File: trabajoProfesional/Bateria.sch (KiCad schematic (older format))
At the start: 28 parts, among them T1 MPMOS

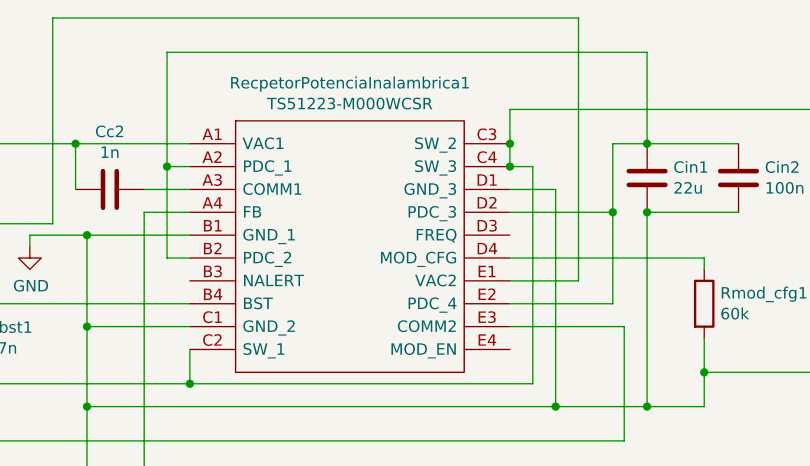
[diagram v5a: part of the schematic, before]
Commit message: achicamiento de placa a un cuarto del tamanio anterior
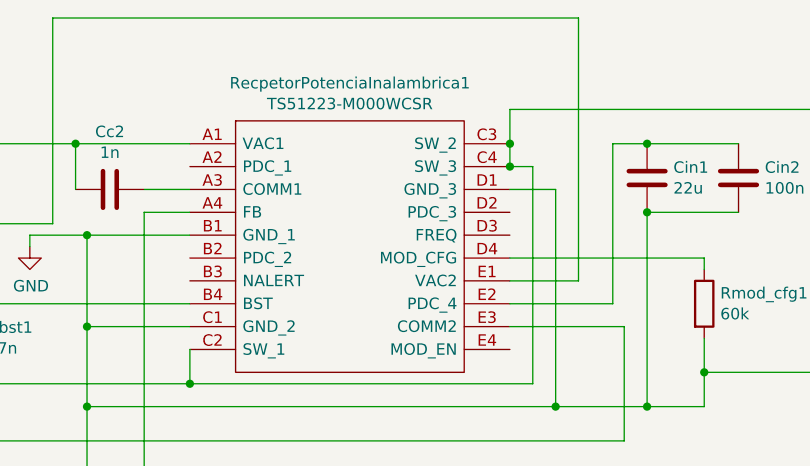
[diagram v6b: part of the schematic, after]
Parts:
- Cbat1, Cvin1: footprint Capacitor_SMD:C_Elec_3x5.4 -> Capacitor_SMD:C_0201_0603Metric
- Cc1, Cc2, Cin1, Cin2, Cout1, Cout2, Cout3, Cout4, Cs2: footprint Capacitor_SMD:CP_Elec_3x5.3 -> Capacitor_SMD:C_0201_0603Metric
- Lout1: footprint Inductor_SMD:L_7.3x7.3_H3.5 -> Inductor_SMD:L_0603_1608Metric_Pad1.05x0.95mm_HandSolder
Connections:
- net at Cin1.2, Cin2.2, RecpetorPotenciaInalambrica1.E2 (PDC_4): no longer RecpetorPotenciaInalambrica1.A2 (PDC_1), RecpetorPotenciaInalambrica1.B2 (PDC_2), RecpetorPotenciaInalambrica1.D2 (PDC_3)
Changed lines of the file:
@@
 F 0 "Cs2" V 1498 2200 50  0000 C CNN
 F 1 "10n" V 1589 2200 50  0000 C CNN
-F 2 "Capacitor_SMD:CP_Elec_3x5.3" H 1788 2050 50  0001 C CNN
+F 2 "Capacitor_SMD:C_0201_0603Metric" H 1788 2050 50  0001 C CNN
 F 3 "~" H 1750 2200 50  0001 C CNN
 	1    1750 2200
@@
 F 0 "Cc1" H 1435 3054 50  0000 R CNN
 F 1 "1n" H 1435 3145 50  0000 R CNN
-F 2 "Capacitor_SMD:CP_Elec_3x5.3" H 1588 2950 50  0001 C CNN
+F 2 "Capacitor_SMD:C_0201_0603Metric" H 1588 2950 50  0001 C CNN
 F 3 "~" H 1550 3100 50  0001 C CNN
 	1    1550 3100
@@
 F 0 "Cc2" V 3202 2400 50  0000 C CNN
 F 1 "1n" V 3111 2400 50  0000 C CNN
-F 2 "Capacitor_SMD:CP_Elec_3x5.3" H 2988 2250 50  0001 C CNN
+F 2 "Capacitor_SMD:C_0201_0603Metric" H 2988 2250 50  0001 C CNN
 F 3 "~" H 2950 2400 50  0001 C CNN
 	1    2950 2400
@@
 F 0 "Cin1" H 5185 2304 50  0000 R CNN
 F 1 "22u" H 5185 2395 50  0000 R CNN
-F 2 "Capacitor_SMD:CP_Elec_3x5.3" H 5338 2200 50  0001 C CNN
+F 2 "Capacitor_SMD:C_0201_0603Metric" H 5338 2200 50  0001 C CNN
 F 3 "~" H 5300 2350 50  0001 C CNN
 	1    5300 2350
@@
 F 0 "Lout1" V 6819 2500 50  0000 C CNN
 F 1 "4.7u" V 6910 2500 50  0000 C CNN
-F 2 "Inductor_SMD:L_7.3x7.3_H3.5" H 7000 2500 50  0001 C CNN
+F 2 "Inductor_SMD:L_0603_1608Metric_Pad1.05x0.95mm_HandSolder" H 7000 2500 50  0001 C CNN
 F 3 "~" H 7000 2500 50  0001 C CNN
 	1    7000 2500
@@
 Wire Wire Line
 	5300 3350 4900 3350
-Wire Wire Line
-	4700 2900 5150 2900
-Wire Wire Line
-	5150 2900 5150 2500
-Wire Wire Line
-	5150 2200 5300 2200
-Wire Wire Line
-	3300 2300 3200 2300
-Wire Wire Line
-	3200 1800 5300 1800
-Wire Wire Line
-	5300 1800 5300 2200
-Wire Wire Line
-	3200 1800 3200 2300
 Connection ~ 5300 2200
-Wire Wire Line
-	3300 2700 3200 2700
-Wire Wire Line
-	3200 2700 3200 2300
-Connection ~ 3200 2300
-Wire Wire Line
-	4700 2500 5150 2500
-Connection ~ 5150 2500
-Wire Wire Line
-	5150 2500 5150 2200
 Wire Wire Line
 	3300 2900 2300 2900
@@
 F 0 "Cin2" H 5585 2304 50  0000 R CNN
 F 1 "100n" H 5585 2395 50  0000 R CNN
-F 2 "Capacitor_SMD:CP_Elec_3x5.3" H 5738 2200 50  0001 C CNN
+F 2 "Capacitor_SMD:C_0201_0603Metric" H 5738 2200 50  0001 C CNN
 F 3 "~" H 5700 2350 50  0001 C CNN
 	1    5700 2350
@@
 F 0 "Cout1" H 7535 2604 50  0000 R CNN
 F 1 "22u" H 7535 2695 50  0000 R CNN
-F 2 "Capacitor_SMD:CP_Elec_3x5.3" H 7688 2500 50  0001 C CNN
+F 2 "Capacitor_SMD:C_0201_0603Metric" H 7688 2500 50  0001 C CNN
 F 3 "~" H 7650 2650 50  0001 C CNN
 	1    7650 2650
@@
 F 0 "Cout2" H 7935 2604 50  0000 R CNN
 F 1 "22u" H 7935 2695 50  0000 R CNN
-F 2 "Capacitor_SMD:CP_Elec_3x5.3" H 8088 2500 50  0001 C CNN
+F 2 "Capacitor_SMD:C_0201_0603Metric" H 8088 2500 50  0001 C CNN
 F 3 "~" H 8050 2650 50  0001 C CNN
 	1    8050 2650
@@
 F 0 "Cout3" H 8335 2604 50  0000 R CNN
 F 1 "22u" H 8335 2695 50  0000 R CNN
-F 2 "Capacitor_SMD:CP_Elec_3x5.3" H 8488 2500 50  0001 C CNN
+F 2 "Capacitor_SMD:C_0201_0603Metric" H 8488 2500 50  0001 C CNN
 F 3 "~" H 8450 2650 50  0001 C CNN
 	1    8450 2650
@@
 F 0 "Cout4" H 8635 2604 50  0000 R CNN
 F 1 "22u" H 8635 2695 50  0000 R CNN
-F 2 "Capacitor_SMD:CP_Elec_3x5.3" H 8788 2500 50  0001 C CNN
+F 2 "Capacitor_SMD:C_0201_0603Metric" H 8788 2500 50  0001 C CNN
 F 3 "~" H 8750 2650 50  0001 C CNN
 	1    8750 2650
@@
 F 0 "Cbat1" H 6265 5296 50  0000 L CNN
 F 1 "2.2u" H 6265 5205 50  0000 L CNN
-F 2 "Capacitor_SMD:C_Elec_3x5.4" H 6188 5100 50  0001 C CNN
+F 2 "Capacitor_SMD:C_0201_0603Metric" H 6188 5100 50  0001 C CNN
 F 3 "~" H 6150 5250 50  0001 C CNN
 	1    6150 5250
@@
 F 0 "Cvin1" V 2848 4750 50  0000 C CNN
 F 1 "2.2u" V 2939 4750 50  0000 C CNN
-F 2 "Capacitor_SMD:C_Elec_3x5.4" H 3138 4600 50  0001 C CNN
+F 2 "Capacitor_SMD:C_0201_0603Metric" H 3138 4600 50  0001 C CNN
 F 3 "~" H 3100 4750 50  0001 C CNN
 	1    3100 4750
@@
 Wire Wire Line
 	7300 5650 6950 5650
+Wire Wire Line
+	4700 2900 5150 2900
+Wire Wire Line
+	5150 2900 5150 2200
+Wire Wire Line
+	5150 2200 5300 2200
 $EndSCHEMATC

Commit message: mira como ponemos todo de una cara
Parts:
- Rstatus1: footprint Resistor_SMD:R_1806_4516Metric -> Resistor_SMD:R_0201_0603Metric
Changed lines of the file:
@@
 F 0 "Rstatus1" V 3843 4500 50  0000 C CNN
 F 1 "R" V 3934 4500 50  0000 C CNN
-F 2 "Resistor_SMD:R_1806_4516Metric" V 3980 4500 50  0001 C CNN
+F 2 "Resistor_SMD:R_0201_0603Metric" V 3980 4500 50  0001 C CNN
 F 3 "~" H 4050 4500 50  0001 C CNN
 	1    4050 4500

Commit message: Add files via upload
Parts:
- AdministracionBateria1: symbol SC810ULTRT:SC810ULTRT -> trabajoProfesional-rescue:SC810ULTRT-SC810ULTRT
- Cc1, Cc2: footprint Capacitor_SMD:C_0201_0603Metric -> Capacitor_SMD:C_0402_1005Metric
- Cs2: footprint Capacitor_SMD:C_0201_0603Metric -> Capacitor_SMD:C_0603_1608Metric
- RIPRGM1, Rstatus1: value R -> 10k
- RecpetorPotenciaInalambrica1: symbol TS51223-M000WCSR:TS51223-M000WCSR -> trabajoProfesional-rescue:TS51223-M000WCSR-TS51223-M000WCSR
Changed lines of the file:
@@
 EESchema Schematic File Version 4
-EELAYER 30 0
+LIBS:trabajoProfesional-cache
+EELAYER 26 0
 EELAYER END
 $Descr A4 11693 8268
@@
 $EndDescr
 $Comp
-L TS51223-M000WCSR:TS51223-M000WCSR RecpetorPotenciaInalambrica1
+L trabajoProfesional-rescue:TS51223-M000WCSR-TS51223-M000WCSR RecpetorPotenciaInalambrica1
 U 1 1 5F3EC0E0
 P 3300 2200
@@
 $EndComp
 $Comp
-L SC810ULTRT:SC810ULTRT AdministracionBateria1
+L trabajoProfesional-rescue:SC810ULTRT-SC810ULTRT AdministracionBateria1
 U 1 1 5F3EDAD5
 P 3500 4950
@@
 F 0 "Cs2" V 1498 2200 50  0000 C CNN
 F 1 "10n" V 1589 2200 50  0000 C CNN
-F 2 "Capacitor_SMD:C_0201_0603Metric" H 1788 2050 50  0001 C CNN
+F 2 "Capacitor_SMD:C_0603_1608Metric" H 1788 2050 50  0001 C CNN
 F 3 "~" H 1750 2200 50  0001 C CNN
 	1    1750 2200
@@
 F 0 "Cc1" H 1435 3054 50  0000 R CNN
 F 1 "1n" H 1435 3145 50  0000 R CNN
-F 2 "Capacitor_SMD:C_0201_0603Metric" H 1588 2950 50  0001 C CNN
+F 2 "Capacitor_SMD:C_0402_1005Metric" H 1588 2950 50  0001 C CNN
 F 3 "~" H 1550 3100 50  0001 C CNN
 	1    1550 3100
@@
 F 0 "Cc2" V 3202 2400 50  0000 C CNN
 F 1 "1n" V 3111 2400 50  0000 C CNN
-F 2 "Capacitor_SMD:C_0201_0603Metric" H 2988 2250 50  0001 C CNN
+F 2 "Capacitor_SMD:C_0402_1005Metric" H 2988 2250 50  0001 C CNN
 F 3 "~" H 2950 2400 50  0001 C CNN
 	1    2950 2400
@@
 P 5100 5200
 F 0 "RIPRGM1" V 4893 5200 50  0000 C CNN
-F 1 "R" V 4984 5200 50  0000 C CNN
+F 1 "10k" V 4984 5200 50  0000 C CNN
 F 2 "Resistor_SMD:R_0201_0603Metric" V 5030 5200 50  0001 C CNN
 F 3 "~" H 5100 5200 50  0001 C CNN
@@
 P 4050 4500
 F 0 "Rstatus1" V 3843 4500 50  0000 C CNN
-F 1 "R" V 3934 4500 50  0000 C CNN
+F 1 "10k" V 3934 4500 50  0000 C CNN
 F 2 "Resistor_SMD:R_0201_0603Metric" V 3980 4500 50  0001 C CNN
 F 3 "~" H 4050 4500 50  0001 C CNN
